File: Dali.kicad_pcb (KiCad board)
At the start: 2 copper layers, 56 parts, among them M1 ESP8266, P1 CONN_01X03, P10 TST, P11 USB_OTG, P2 CONN_01X02, P3 CONN_01X02, P4 TST, P5 TST, P6 TST, P7 TST, P8 TST, P9 TST, Q1 BC546, Q2 S8050, Q3 S8050, SW1 SW_PUSH, T1 TRANSFO, U1 MCP2003, U2 MC34063, U3 CRD, U4 FT232RL, X1 QUARTZ

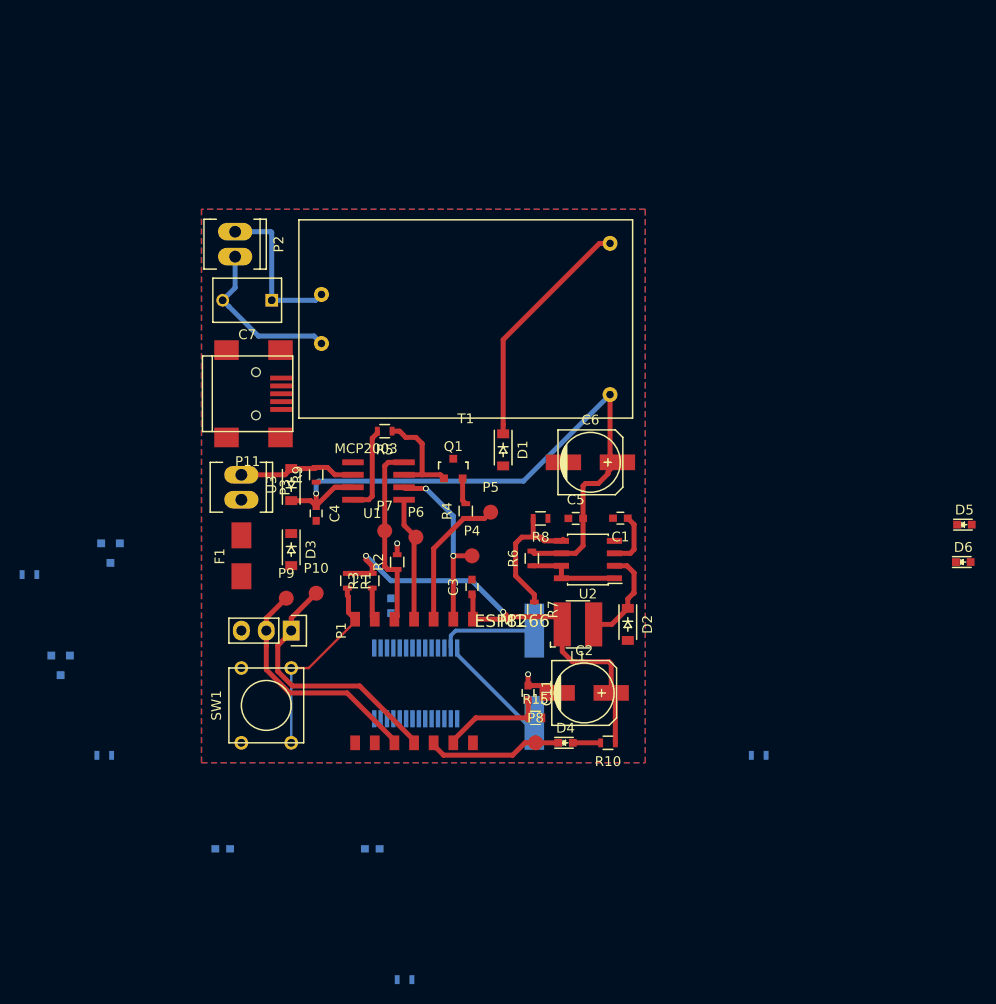
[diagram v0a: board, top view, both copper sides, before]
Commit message: working on version. before changing voltage regulator
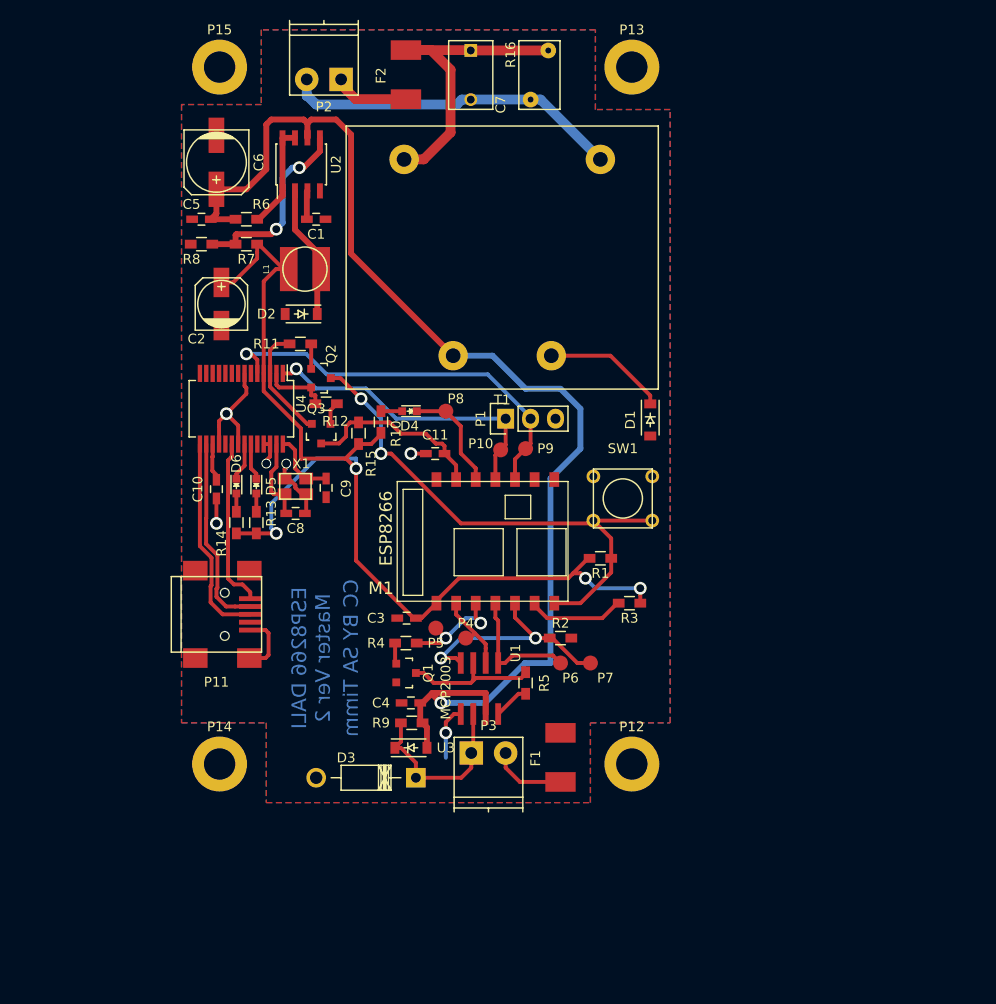
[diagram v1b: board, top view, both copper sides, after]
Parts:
- added F2: FUSE, Fuse_TE:FUSE_2410, F.Cu at (126.0, 48.8)
- added P12: CONN_01X01, Mounting_Holes:MountingHole_3.2mm_M3_DIN965_Pad, F.Cu at (149.0, 119.0)
- added P13: CONN_01X01, Mounting_Holes:MountingHole_3.2mm_M3_DIN965_Pad, F.Cu at (149.0, 48.0)
- added P14: CONN_01X01, Mounting_Holes:MountingHole_3.2mm_M3_DIN965_Pad, F.Cu at (107.0, 119.0)
- added P15: CONN_01X01, Mounting_Holes:MountingHole_3.2mm_M3_DIN965_Pad, F.Cu at (107.0, 48.0)
- added R16: RVAR, Varistors:RV_Disc_D7_W4.2_P5, F.Cu at (140.5, 46.3)
- C1: value C -> 470p; footprint Capacitors_SMD:C_0603 -> Capacitors_SMD:C_0603_HandSoldering
- C10, C8, C9: footprint Capacitors_SMD:C_0603 -> Capacitors_SMD:C_0603_HandSoldering; moved to F.Cu
- C11: value C -> 470pF; footprint Capacitors_SMD:C_0603 -> Capacitors_SMD:C_0603_HandSoldering
- C2: footprint Capacitors_SMD:c_elec_6.3x7.7 -> Capacitors_SMD:c_elec_5x5.3
- C3: value C -> 100nF; footprint Capacitors_SMD:C_0603 -> Capacitors_SMD:C_0603_HandSoldering
- C4: footprint Capacitors_SMD:C_0603 -> Capacitors_SMD:C_0603_HandSoldering
- C5: value C -> 100n; footprint Capacitors_SMD:C_0603 -> Capacitors_SMD:C_0603_HandSoldering
- D3: footprint Diodes_SMD:SOD-123 -> Diodes_ThroughHole:Diode_DO-41_SOD81_Horizontal_RM10
- F1: footprint Fuse_Holders_and_Fuses:Fuse_SMD1206_HandSoldering -> Fuse_TE:FUSE_2410
- L1: footprint CD43:CD43 -> SDR0403:BOURNS-SDR0403
- M1: footprint ESP:ESP8266-ESP-03 -> ESP8266:ESP8266-ESP-03
- P2, P3: footprint Sockets_MOLEX_KK-System:Socket_MOLEX-KK-RM2-54mm_Lock_2pin_straight -> Stecker:TerminalBlock_Pheonix_PT-3.5mm_2pol
- Q1: value BC546 -> Q_NPN_BEC
- Q2, Q3: value S8050 -> Q_NPN_BEC; moved to F.Cu
- R1, R15, R2, R3: value R -> 12k; footprint Resistors_SMD:R_0603 -> Resistors_SMD:R_0603_HandSoldering
- R10: value R -> 330; footprint Resistors_SMD:R_0603 -> Resistors_SMD:R_0603_HandSoldering
- R11, R12: value R -> 12K; footprint Resistors_SMD:R_0603 -> Resistors_SMD:R_0603_HandSoldering; moved to F.Cu
- R13, R14: value R -> 330; footprint Resistors_SMD:R_0603 -> Resistors_SMD:R_0603_HandSoldering; moved to F.Cu
- R4, R5, R9: footprint Resistors_SMD:R_0603 -> Resistors_SMD:R_0603_HandSoldering
- R6: value R -> 1; footprint Resistors_SMD:R_0603 -> Resistors_SMD:R_0603_HandSoldering
- R7: value R -> 1,8k; footprint Resistors_SMD:R_0603 -> Resistors_SMD:R_0603_HandSoldering
- R8: value R -> 1k; footprint Resistors_SMD:R_0603 -> Resistors_SMD:R_0603_HandSoldering
- SW1: footprint Buttons_Switches_ThroughHole:SW_PUSH_SMALL -> Taster:SW_PUSH_SMALL
- T1: footprint HLK_PM12:HLK_PM12 -> VTX-214-003-115:VTX-214-003-115
- U4: moved to F.Cu
- X1: value QUARTZ -> CRYSTAL_SMD; footprint Crystals:Q_49U3HMS -> Crystals:crystal_FA238-TSX3225; moved to F.Cu
- moved D6 74.5 mm to (108.7, 90.7), turned to 270 degrees
- moved D5 72.2 mm to (110.7, 90.7), turned to 270 degrees
- moved R13 56.4 mm to (110.7, 94.4), turned to 270 degrees
- moved C2 54.2 mm to (107.2, 72.1), turned to 90 degrees
- moved U2 49.7 mm to (115.3, 57.9), turned to 90 degrees
- moved R14 49.6 mm to (108.7, 94.4), turned to 270 degrees
- moved C6 48.8 mm to (106.7, 57.7), turned to 270 degrees
- moved C5 48.8 mm to (105.2, 63.5)
- moved R7 47.4 mm to (109.7, 66.0), turned to 0 degrees
- moved R11 46.4 mm to (115.2, 76.2)
- moved D2 45.9 mm to (115.3, 73.2), turned to 180 degrees
- moved L1 45.6 mm to (115.7, 68.6), turned to 90 degrees
- moved R6 45.2 mm to (109.7, 63.5), turned to 180 degrees
- moved R8 44.4 mm to (105.2, 66.0), turned to 0 degrees
- moved C1 43.5 mm to (116.8, 63.5), turned to 0 degrees
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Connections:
- M1 pad ANT: Net-(M1-PadANT) -> (no net)
- M1 pad NC: Net-(M1-PadNC) -> (no net)
- M1 pad URXD: Net-(M1-PadURXD) -> URXD
- M1 pad UTXD: Net-(M1-PadUTXD) -> UTXD
- P1 pad 1: Net-(M1-PadURXD) -> URXD
- P1 pad 2: Net-(M1-PadUTXD) -> UTXD
- P10 pad 1: Net-(M1-PadURXD) -> URXD
- P11 pad 4: Net-(P11-Pad4) -> (no net)
- P2 pad 1: Net-(C7-Pad1) -> Net-(F2-Pad2)
- P9 pad 1: Net-(M1-PadUTXD) -> UTXD
- Q1 pad 2: Net-(Q1-Pad2) -> GND
- Q1 pad 3: GND -> Net-(Q1-Pad3)
- R11 pad 1: Net-(Q3-Pad1) -> Net-(Q3-Pad2)
- R11 pad 2: Net-(Q2-Pad2) -> Net-(Q2-Pad1)
- R12 pad 1: Net-(Q2-Pad1) -> Net-(Q2-Pad2)
- R12 pad 2: Net-(Q3-Pad2) -> Net-(Q3-Pad1)
- R4 pad 2: Net-(Q1-Pad2) -> Net-(Q1-Pad1)
- R5 pad 1: Net-(Q1-Pad1) -> Net-(Q1-Pad3)
- T1 pad 1: Net-(C7-Pad1) -> Net-(C7-Pad2)
- T1 pad 2: Net-(C7-Pad2) -> Net-(C7-Pad1)
- T1 pad 3: Net-(D1-Pad1) -> Net-(C4-Pad1)
- T1 pad 4: Net-(C4-Pad1) -> Net-(D1-Pad1)
- U1 pad 3: Net-(Q1-Pad1) -> Net-(Q1-Pad3)
- U3 pad 1: Net-(C4-Pad1) -> Net-(D3-Pad1)
- U3 pad 2: Net-(D3-Pad1) -> Net-(C4-Pad1)
- U4 pad 1: RXD -> URXD
- U4 pad 10: Net-(U4-Pad10) -> (no net)
- U4 pad 11: Net-(U4-Pad11) -> (no net)
- U4 pad 12: Net-(U4-Pad12) -> (no net)
- U4 pad 13: Net-(U4-Pad13) -> (no net)
- U4 pad 14: Net-(U4-Pad14) -> (no net)
- U4 pad 19: Net-(U4-Pad19) -> (no net)
- U4 pad 2: Net-(Q2-Pad1) -> Net-(Q2-Pad2)
- U4 pad 3: Net-(Q3-Pad1) -> Net-(Q3-Pad2)
- U4 pad 5: TXD -> UTXD
- U4 pad 6: Net-(U4-Pad6) -> (no net)
- U4 pad 9: Net-(U4-Pad9) -> (no net)
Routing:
- net +3V3: track 50.8 -> 110.6 mm, vias 2 -> 4
- net Net-(C4-Pad1): track 68.7 -> 125.8 mm
- net UTXD: track 0.00 -> 41.4 mm, vias 0 -> 1
- net FLASH: track 19.8 -> 54.2 mm, vias 0 -> 2
- net GND: track 5.58 -> 38.3 mm, vias 2 -> 6
- net URXD: track 0.00 -> 31.6 mm, vias 0 -> 1
- net Net-(M1-PadURXD): track 26.6 -> 0.00 mm
- net Net-(M1-PadUTXD): track 24.6 -> 0.00 mm
- net Net-(P11-Pad3): track 0.00 -> 21.2 mm
- net Net-(P11-Pad2): track 0.00 -> 19.9 mm
- net Net-(C7-Pad2): track 16.9 -> 34.7 mm
- net +5V: track 0.00 -> 17.4 mm
- net Net-(C7-Pad1): track 16.0 -> 32.2 mm
- net Net-(Q1-Pad3): track 0.00 -> 13.9 mm
- net Net-(D1-Pad1): track 24.5 -> 12.6 mm
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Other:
- net class 230V added: clearance 2, trace_width 1, via_dia 1.3, via_drill 0.8
- net class Default: trace_width 0.508 -> 0.4; via_dia 0.6 -> 1.3; via_drill 0.4 -> 0.8
- net class POWER added: clearance 0.2, trace_width 0.6, via_dia 1.3, via_drill 0.8
- net class SMALL removed
- board text added: "CC BY SA Timm"
- board text added: "ESP8266 DALI Master Ver 2"

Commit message: latest production state
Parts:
- removed U2: MC34063, Housings_SOIC:SOIC-8_3.9x4.9mm_Pitch1.27mm
- added C12: CP, Capacitors_SMD:c_elec_5x5.3, F.Cu at (117.3, 111.3)
- added D7: D_Schottky, Diodes_SMD:SOD-123, F.Cu at (110.7, 63.5)
- added D8: D_Schottky, Diodes_SMD:SOD-123, F.Cu at (115.2, 98.0)
- added IC1: LMR14206, TO_SOT_Packages_SMD:SOT-23-6, F.Cu at (106.7, 57.9)
- added R17: 10k, Resistors_SMD:R_0603_HandSoldering, F.Cu at (109.2, 53.8)
- C1: value 470p -> 100n
- C4: value C -> 220p
- C5: value 100n -> CP; footprint Capacitors_SMD:C_0603_HandSoldering -> Capacitors_SMD:c_elec_5x5.3
- R16: footprint Varistors:RV_Disc_D7_W4.2_P5 -> Varistors_Own:RV_Disc_D7_W4.2_P5_Big
- R6: value 1 -> 4,7k
- R7: value 1,8k -> 2k
- R8: value 1k -> 34k
- moved C5 42.4 mm to (117.3, 104.1)
- moved R8 12.2 mm to (105.7, 53.8), turned to 90 degrees
- moved C6 9.37 mm to (115.8, 59.7)
- moved C1 8.61 mm to (110.2, 58.0), turned to 270 degrees
- moved R6 3.21 mm to (106.7, 62.5), turned to 0 degrees
- moved R7 3.01 mm to (106.8, 65.5)
- moved R5 0.51 mm to (138.2, 111.3)
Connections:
- C1 pad 2: GND -> Net-(C1-Pad2)
- C5 pad 1: GND -> +3V3
- C5 pad 2: Net-(C4-Pad1) -> GND
- D2 pad 1: Net-(D2-Pad1) -> Net-(C1-Pad2)
- L1 pad 2: Net-(D2-Pad1) -> Net-(C1-Pad2)
- R6 pad 1: Net-(R6-Pad1) -> Net-(IC1-Pad4)
- R7 pad 1: Net-(R7-Pad1) -> GND
- R7 pad 2: +3V3 -> Net-(IC1-Pad4)
- R8 pad 1: GND -> Net-(IC1-Pad3)
- R8 pad 2: Net-(R7-Pad1) -> +3V3
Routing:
- net +3V3: track 110.6 -> 146.4 mm
- net Net-(C1-Pad2): track 0.00 -> 25.0 mm, vias 0 -> 2
- net Net-(C4-Pad1): track 125.8 -> 104.9 mm
- net Net-(R7-Pad1): track 19.5 -> 0.00 mm, vias 2 -> 0
- net Net-(D2-Pad1): track 13.8 -> 0.00 mm
- net Net-(R6-Pad1): track 10.7 -> 0.00 mm
- net GND: track 38.3 -> 46.4 mm, vias 6 -> 7
- net Net-(IC1-Pad4): track 0.00 -> 7.62 mm
- net +5V: track 17.4 -> 23.5 mm
- net Net-(C1-Pad1): track 2.91 -> 8.05 mm
- net Net-(IC1-Pad3): track 0.00 -> 4.80 mm
